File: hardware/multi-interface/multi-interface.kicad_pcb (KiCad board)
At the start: 2 copper layers, 70 x 30 mm, 24 parts, among them J1 RJ45, J2 RJ45, J3 RJ45, J4 RJ45, P1 CONN_4X2, P2 CONN_2, P3 CONN_2, P4 CONN_1, P5 CONN_1, P6 CONN_1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

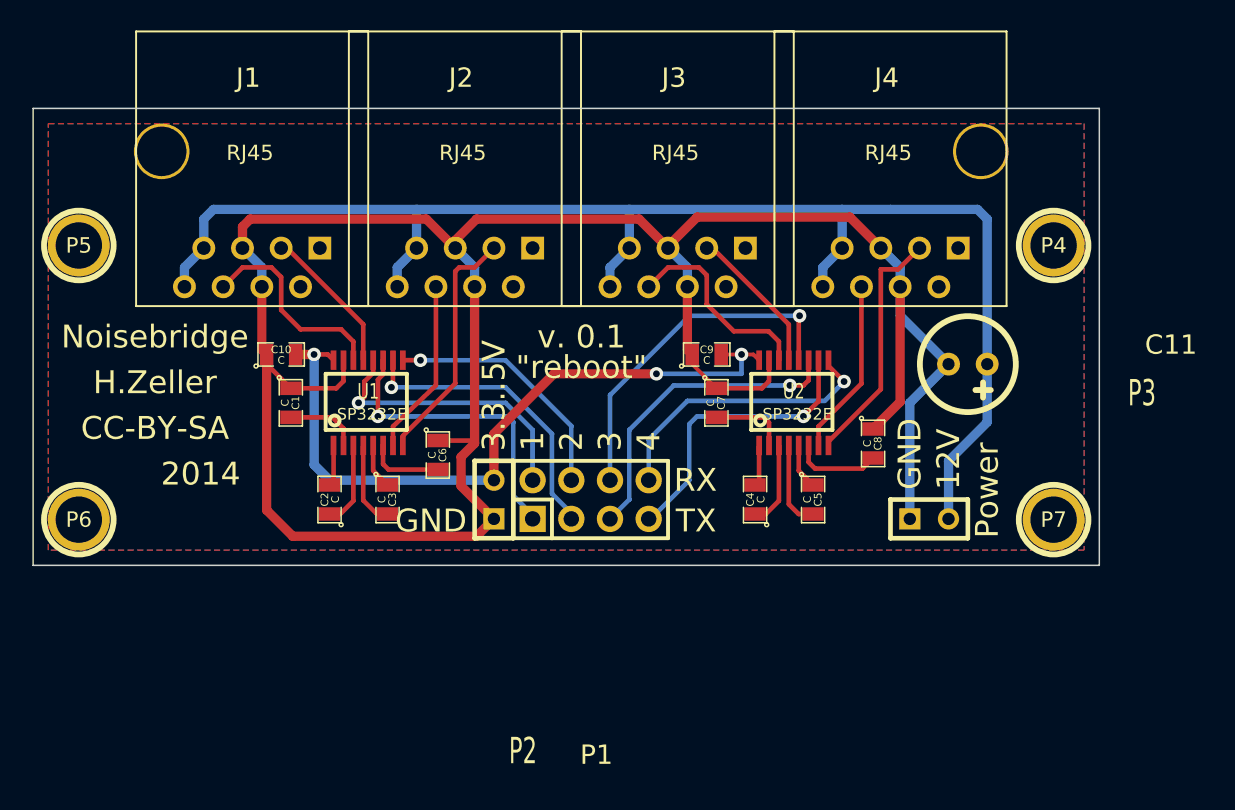
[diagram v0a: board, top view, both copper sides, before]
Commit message: o make 12v powertrace slightly wider.
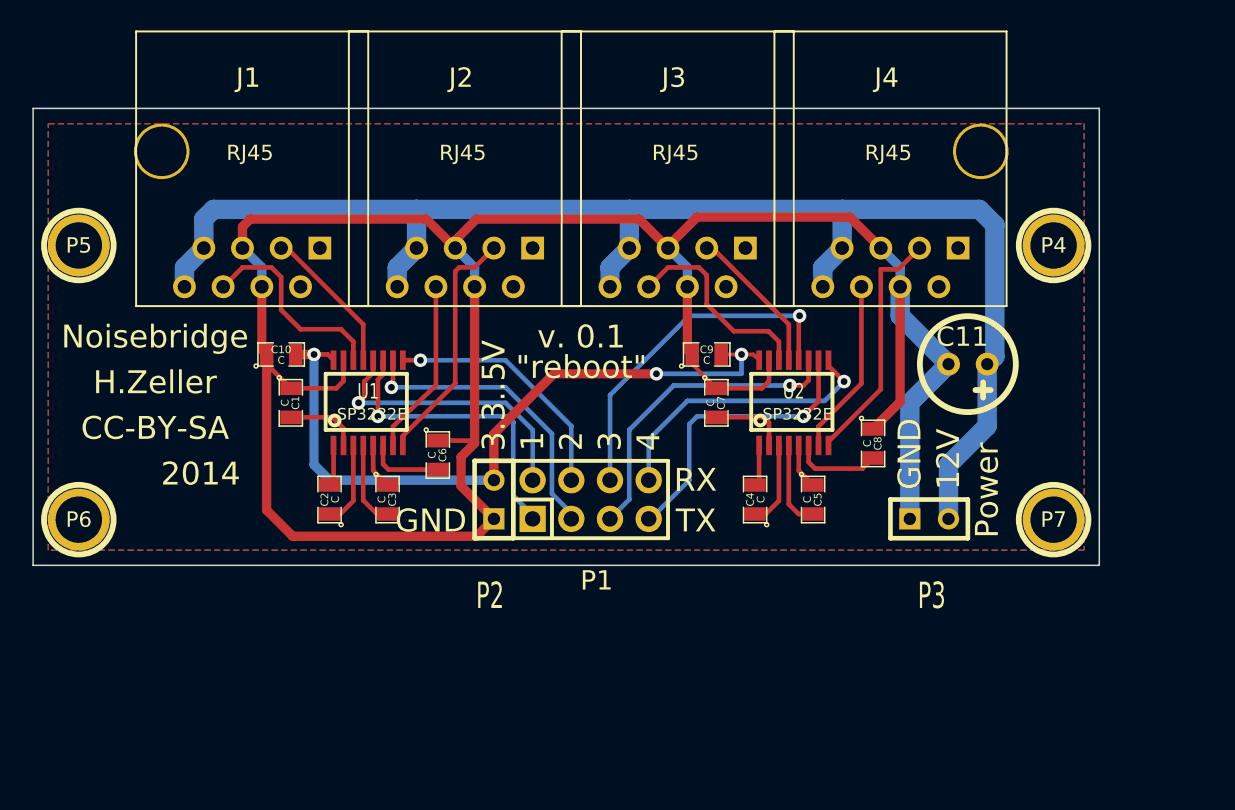
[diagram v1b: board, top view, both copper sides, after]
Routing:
- net GND: track 158.7 -> 170.8 mm
- net +12V: track 94.5 -> 102.0 mm
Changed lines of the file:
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@@
     (links 59)
     (no_connects 0)
-    (area 104.694372 75.679299 182.274029 124.756418)
+    (area 104.694372 75.679299 175.305629 114.566418)
     (thickness 1.6)
     (drawings 22)
-    (tracks 224)
+    (tracks 231)
     (zones 0)
     (modules 24)
@@
   )
   (setup
-    (last_trace_width 0.254)
+    (last_trace_width 1.27)
     (user_trace_width 0.254)
     (user_trace_width 0.3048)
     (user_trace_width 0.6096)
+    (user_trace_width 1.27)
     (trace_clearance 0.2032)
     (zone_clearance 0.508)
@@
     (descr "Electrolytic Capacitor, vertical, diameter 6,3mm, RM 2,5mm, radial,")
     (tags "Electrolytic Capacitor, vertical, diameter 6,3mm, RM 2,5mm, Elko, Electrolytkondensator, Kondensator gepolt, Durchmesser 6,3mm, radial,")
-    (fp_text reference C11 (at -13.335 1.27 180) (layer F.SilkS)
+    (fp_text reference C11 (at 0.37 1.79 180) (layer F.SilkS)
       (effects (font (thickness 0.3048)))
     )
@@
     (descr "1 pin")
     (tags "CONN DEV")
-    (fp_text reference P1 (at 0.381 16.764) (layer F.SilkS)
+    (fp_text reference P1 (at 0.395 5.32) (layer F.SilkS)
       (effects (font (size 1.27 1.27) (thickness 0.2032)))
     )
@@
     (descr "Connecteurs 2 pins")
     (tags "CONN DEV")
-    (fp_text reference P2 (at -16.51 1.905 180) (layer F.SilkS)
+    (fp_text reference P2 (at -6.32 -0.255 180) (layer F.SilkS)
       (effects (font (size 1.72974 1.08712) (thickness 0.3048)))
     )
@@
     (descr "Connecteurs 2 pins")
     (tags "CONN DEV")
-    (fp_text reference P3 (at 13.97 -8.255) (layer F.SilkS)
+    (fp_text reference P3 (at 0.17 5.05) (layer F.SilkS)
       (effects (font (size 1.72974 1.08712) (thickness 0.3048)))
     )
@@
   (gr_line (start 175 81) (end 175 111) (angle 90) (layer Edge.Cuts) (width 0.1))
   (gr_line (start 105 81) (end 175 81) (angle 90) (layer Edge.Cuts) (width 0.1))
+  (segment (start 165.1 97.79) (end 162.56 100.33) (width 1.27) (layer B.Cu) (net 1))
+  (segment (start 162.56 100.33) (end 162.56 107.95) (width 1.27) (layer B.Cu) (net 1))
+  (segment (start 161.925 92.71) (end 161.925 94.615) (width 1.27) (layer B.Cu) (net 1))
+  (segment (start 161.925 94.615) (end 165.1 97.79) (width 1.27) (layer B.Cu) (net 1))
   (segment (start 122.047 109.093) (end 134.112 109.093) (width 0.6096) (layer F.Cu) (net 1))
   (segment (start 134.112 109.093) (end 135.255 107.95) (width 0.6096) (layer F.Cu) (net 1))
@@
   (segment (start 161.925 92.71) (end 161.925 100.2665) (width 0.6096) (layer F.Cu) (net 1))
   (segment (start 161.925 94.615) (end 165.1 97.79) (width 0.6096) (layer B.Cu) (net 1))
-  (segment (start 161.925 92.71) (end 161.925 94.615) (width 0.6096) (layer B.Cu) (net 1))
   (segment (start 162.56 100.33) (end 162.56 107.95) (width 0.6096) (layer B.Cu) (net 1))
-  (segment (start 165.1 97.79) (end 162.56 100.33) (width 0.6096) (layer B.Cu) (net 1))
   (segment (start 121.92 101.2825) (end 124.6505 101.2825) (width 0.3048) (layer F.Cu) (net 2))
   (segment (start 125.3744 102.0064) (end 125.3744 103.12908) (width 0.3048) (layer F.Cu) (net 2))
@@
   (segment (start 135.255 105.41) (end 135.255 102.362) (width 0.6096) (layer F.Cu) (net 14))
   (via (at 151.511 97.155) (size 0.889) (layers F.Cu B.Cu) (net 14))
+  (segment (start 158.115 90.17) (end 156.845 91.44) (width 1.27) (layer B.Cu) (net 15))
+  (segment (start 156.845 91.44) (end 156.845 92.71) (width 1.27) (layer B.Cu) (net 15))
+  (segment (start 144.145 90.17) (end 142.875 91.44) (width 1.27) (layer B.Cu) (net 15))
+  (segment (start 142.875 91.44) (end 142.875 92.71) (width 1.27) (layer B.Cu) (net 15))
+  (segment (start 130.175 90.17) (end 128.905 91.44) (width 1.27) (layer B.Cu) (net 15))
+  (segment (start 128.905 91.44) (end 128.905 92.71) (width 1.27) (layer B.Cu) (net 15))
+  (segment (start 116.205 90.17) (end 114.935 91.44) (width 1.27) (layer B.Cu) (net 15))
+  (segment (start 114.935 91.44) (end 114.935 92.71) (width 1.27) (layer B.Cu) (net 15))
+  (segment (start 167.64 97.79) (end 167.64 101.854) (width 1.27) (layer B.Cu) (net 15))
+  (segment (start 165.1 104.394) (end 165.1 107.95) (width 1.27) (layer B.Cu) (net 15))
+  (segment (start 167.64 101.854) (end 165.1 104.394) (width 1.27) (layer B.Cu) (net 15))
+  (segment (start 158.115 87.63) (end 167.132 87.63) (width 1.27) (layer B.Cu) (net 15))
+  (segment (start 168.148 88.646) (end 168.148 97.282) (width 1.27) (layer B.Cu) (net 15))
+  (segment (start 167.132 87.63) (end 168.148 88.646) (width 1.27) (layer B.Cu) (net 15))
+  (segment (start 168.148 97.282) (end 167.64 97.79) (width 1.27) (layer B.Cu) (net 15))
+  (segment (start 158.115 87.63) (end 158.115 90.17) (width 1.27) (layer B.Cu) (net 15))
+  (segment (start 144.145 87.63) (end 158.115 87.63) (width 1.27) (layer B.Cu) (net 15))
+  (segment (start 144.145 87.63) (end 144.145 90.17) (width 1.27) (layer B.Cu) (net 15))
+  (segment (start 130.175 87.63) (end 144.145 87.63) (width 1.27) (layer B.Cu) (net 15))
+  (segment (start 130.175 87.63) (end 130.175 90.17) (width 1.27) (layer B.Cu) (net 15))
+  (segment (start 116.84 87.63) (end 116.205 88.265) (width 1.27) (layer B.Cu) (net 15))
+  (segment (start 116.205 88.265) (end 116.205 90.17) (width 1.27) (layer B.Cu) (net 15))
+  (segment (start 116.84 87.63) (end 130.175 87.63) (width 1.27) (layer B.Cu) (net 15))
+  (segment (start 116.205 90.17) (end 116.205 88.265) (width 0.6096) (layer B.Cu) (net 15))
   (segment (start 156.845 92.71) (end 156.845 91.44) (width 0.6096) (layer B.Cu) (net 15))
-  (segment (start 156.845 91.44) (end 158.115 90.17) (width 0.6096) (layer B.Cu) (net 15))
-  (segment (start 158.115 90.17) (end 158.115 87.63) (width 0.6096) (layer B.Cu) (net 15))
   (segment (start 142.875 92.71) (end 142.875 91.44) (width 0.6096) (layer B.Cu) (net 15))
-  (segment (start 142.875 91.44) (end 144.145 90.17) (width 0.6096) (layer B.Cu) (net 15))
-  (segment (start 144.145 90.17) (end 144.145 87.63) (width 0.6096) (layer B.Cu) (net 15))
   (segment (start 128.905 92.71) (end 128.905 91.44) (width 0.6096) (layer B.Cu) (net 15))
-  (segment (start 128.905 91.44) (end 130.175 90.17) (width 0.6096) (layer B.Cu) (net 15))
-  (segment (start 130.175 90.17) (end 130.175 87.63) (width 0.6096) (layer B.Cu) (net 15))
   (segment (start 114.935 92.71) (end 114.935 91.44) (width 0.6096) (layer B.Cu) (net 15))
-  (segment (start 114.935 91.44) (end 116.205 90.17) (width 0.6096) (layer B.Cu) (net 15))
-  (segment (start 116.205 90.17) (end 116.205 88.265) (width 0.6096) (layer B.Cu) (net 15))
-  (segment (start 116.205 88.265) (end 116.84 87.63) (width 0.6096) (layer B.Cu) (net 15))
-  (segment (start 116.84 87.63) (end 130.175 87.63) (width 0.6096) (layer B.Cu) (net 15))
-  (segment (start 130.175 87.63) (end 144.145 87.63) (width 0.6096) (layer B.Cu) (net 15))
-  (segment (start 144.145 87.63) (end 158.115 87.63) (width 0.6096) (layer B.Cu) (net 15))
-  (segment (start 167.005 87.63) (end 167.64 88.265) (width 0.6096) (layer B.Cu) (net 15))
-  (segment (start 167.64 88.265) (end 167.64 97.79) (width 0.6096) (layer B.Cu) (net 15))
-  (segment (start 158.115 87.63) (end 161.29 87.63) (width 0.6096) (layer B.Cu) (net 15))
-  (segment (start 161.29 87.63) (end 167.005 87.63) (width 0.6096) (layer B.Cu) (net 15))
-  (segment (start 167.64 101.6) (end 165.1 104.14) (width 0.6096) (layer B.Cu) (net 15))
-  (segment (start 165.1 104.14) (end 165.1 107.95) (width 0.6096) (layer B.Cu) (net 15))
-  (segment (start 167.64 97.79) (end 167.64 101.6) (width 0.6096) (layer B.Cu) (net 15))
   (segment (start 121.285 90.17) (end 121.666 90.17) (width 0.3048) (layer F.Cu) (net 18))
   (segment (start 121.666 90.17) (end 126.67488 95.17888) (width 0.3048) (layer F.Cu) (net 18))

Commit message: o Re-connect with current KiCad library. o add cache to repository to make sure this is kept.
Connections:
- net +3.3V renamed +3V3
- J1 pad 1: Net-(J1-Pad1) -> (no net)
- J1 pad 2: Net-(J1-Pad2) -> (no net)
- J2 pad 1: Net-(J2-Pad1) -> (no net)
- J2 pad 2: Net-(J2-Pad2) -> (no net)
- J3 pad 1: Net-(J3-Pad1) -> (no net)
- J3 pad 2: Net-(J3-Pad2) -> (no net)
- J4 pad 1: Net-(J4-Pad1) -> (no net)
- J4 pad 2: Net-(J4-Pad2) -> (no net)
- P4 pad 1: Net-(P4-Pad1) -> (no net)
- P5 pad 1: Net-(P5-Pad1) -> (no net)
- P6 pad 1: Net-(P6-Pad1) -> (no net)
- P7 pad 1: Net-(P7-Pad1) -> (no net)
